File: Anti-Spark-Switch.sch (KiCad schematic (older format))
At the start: 17 parts, among them P1 Pad_Conn, P2 Pad_Conn, P3 Screw_Terminal, P4 Screw_Terminal, P5 Pad_Conn, P6 Pad_Conn, P7 CONN_01X04, Q1 IRFS7530, Q2 IRFS7530, Q3 IRFS7530

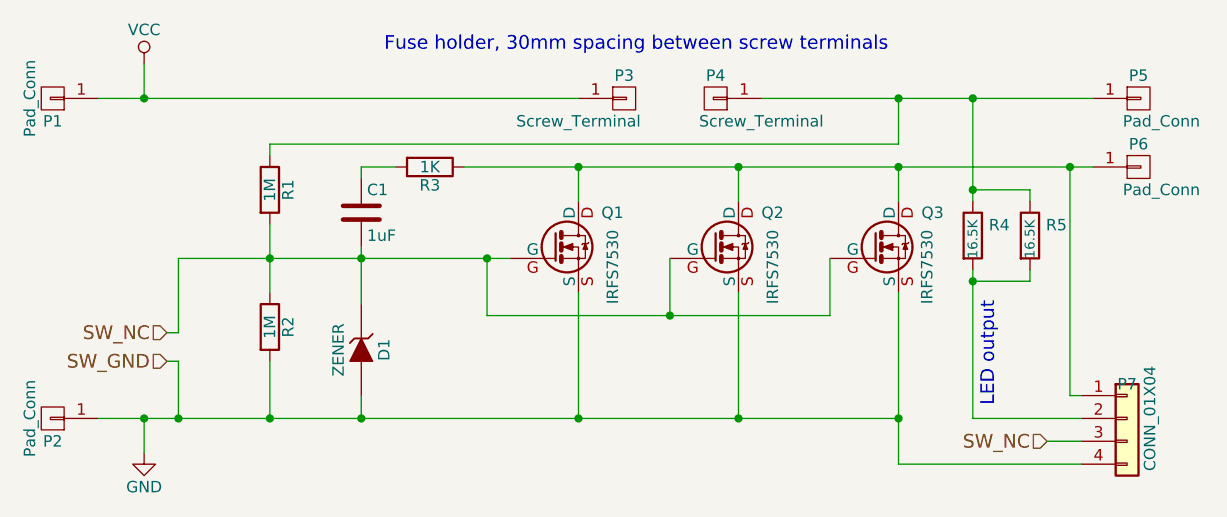
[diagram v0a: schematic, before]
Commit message: removed fuse, changed board size, tweaked layout
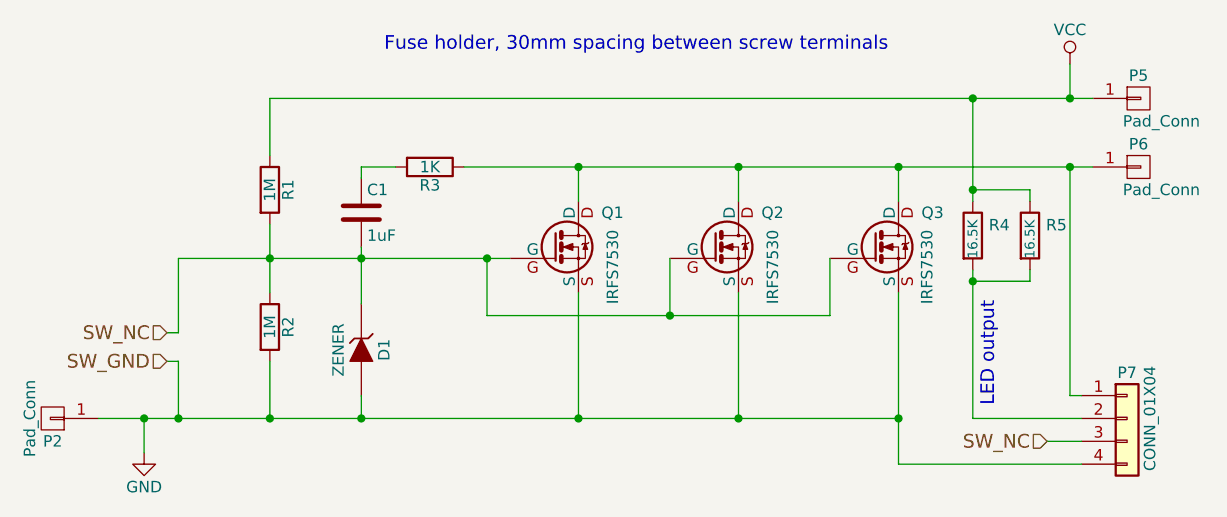
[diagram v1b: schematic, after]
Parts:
- removed P1: Pad_Conn, sparkparts:1PAD_8x7mm, symbol Pad_Conn
- removed P3, P4: Screw_Terminal, sparkparts:M5_Screw_Terminal_12_pin, symbol Screw_Terminal
- P5: footprint sparkparts:1PAD_8x7mm -> Connector_PinHeader_2.54mm:PinHeader_1x01_P2.54mm_Vertical
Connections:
- net VCC: now also P5.1 (P1), R1.1, R4.1, R5.1
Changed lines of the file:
@@
 L VCC #PWR02
 U 1 1 5775E532
-P 4100 2900
-F 0 "#PWR02" H 4100 2750 50  0001 C CNN
-F 1 "VCC" H 4100 3050 50  0000 C CNN
-F 2 "" H 4100 2900 50  0000 C CNN
-F 3 "" H 4100 2900 50  0000 C CNN
-	1    4100 2900
+P 8150 2900
+F 0 "#PWR02" H 8150 2750 50  0001 C CNN
+F 1 "VCC" H 8150 3050 50  0000 C CNN
+F 2 "" H 8150 2900 50  0000 C CNN
+F 3 "" H 8150 2900 50  0000 C CNN
+	1    8150 2900
 	1    0    0    -1
 $EndComp
@@
 U 1 1 577ECAA0
 P 8400 4450
-F 0 "P7" H 8400 4600 50  0000 C CNN
+F 0 "P7" H 8400 4650 50  0000 C CNN
 F 1 "CONN_01X04" V 8500 4450 50  0000 C CNN
 F 2 "Connector_JST:JST_PH_B4B-PH-K_1x04_P2.00mm_Vertical" H 8400 4450 50  0001 C CNN
@@
 	1    0    0    -1
 $EndComp
-$Comp
-L Screw_Terminal P3
-U 1 1 577ECE79
-P 6200 3050
-F 0 "P3" H 6200 3150 50  0000 C CNN
-F 1 "Screw_Terminal" H 6000 2950 50  0000 C CNN
-F 2 "sparkparts:M5_Screw_Terminal_12_pin" H 6200 3050 50  0001 C CNN
-F 3 "" H 6200 3050 50  0000 C CNN
-	1    6200 3050
-	1    0    0    -1
-$EndComp
-$Comp
-L Screw_Terminal P4
-U 1 1 577ECEBD
-P 6600 3050
-F 0 "P4" H 6600 2950 50  0000 C CNN
-F 1 "Screw_Terminal" H 6400 3150 50  0000 C CNN
-F 2 "sparkparts:M5_Screw_Terminal_12_pin" H 6600 3050 50  0001 C CNN
-F 3 "" H 6600 3050 50  0000 C CNN
-	1    6600 3050
-	-1   0    0    1
-$EndComp
 Text Notes 5150 2850 0    60   ~ 0
 Fuse holder, 30mm spacing between screw terminals\n
-$Comp
-L Pad_Conn P1
-U 1 1 577ED8F0
-P 3700 3050
-F 0 "P1" H 3700 3150 50  0000 C CNN
-F 1 "Pad_Conn" V 3800 3050 50  0000 C CNN
-F 2 "sparkparts:1PAD_8x7mm" H 3700 3050 50  0001 C CNN
-F 3 "" H 3700 3050 50  0000 C CNN
-	1    3700 3050
-	-1   0    0    1
-$EndComp
 $Comp
 L Pad_Conn P2
@@
 F 0 "P5" H 8450 3150 50  0000 C CNN
 F 1 "Pad_Conn" H 8550 2950 50  0000 C CNN
-F 2 "sparkparts:1PAD_8x7mm" H 8450 3050 50  0001 C CNN
+F 2 "Connector_PinHeader_2.54mm:PinHeader_1x01_P2.54mm_Vertical" H 8450 3050 50  0001 C CNN
 F 3 "" H 8450 3050 50  0000 C CNN
 	1    8450 3050
@@
 SW_NC
 Wire Wire Line
-	4100 2900 4100 3050
-Wire Wire Line
-	3900 3050 6000 3050
+	8150 3050 8150 2900
 Wire Wire Line
 	4250 3750 5700 3750
@@
 Connection ~ 5600 3750
 Connection ~ 6000 3350
-Wire Wire Line
-	6800 3050 8250 3050
-Connection ~ 4100 3050
 Connection ~ 4100 4450
 Wire Wire Line
-	7400 3050 7400 3250
-Wire Wire Line
-	7400 3250 4650 3250
-Wire Wire Line
-	4650 3250 4650 3300
-Connection ~ 7400 3050
+	4650 3050 4650 3300
 Wire Wire Line
 	3900 4450 7400 4450
@@
 	7400 4650 8200 4650
 Connection ~ 7400 4450
+Wire Wire Line
+	4650 3050 8250 3050
+Connection ~ 8150 3050
 $EndSCHEMATC
